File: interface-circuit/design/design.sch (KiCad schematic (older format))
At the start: 28 parts, among them J1 Raspberry_Pi_2_3, J10 Screw_Terminal_01x02, J11 Conn_01x02_Male, J12 Conn_01x02_Male, J2 Screw_Terminal_01x05, J3 Screw_Terminal_01x05, J4 Screw_Terminal_01x02, J5 Conn_01x02_Male, J6 Conn_01x02_Male, J7 Conn_01x03_Male, J8 Conn_01x03_Male, J9 Screw_Terminal_01x02, Q1 2N3904-AP, Q2 2N3904-AP, Q3 2N3904-AP, SW1 SW_SPST, SW2 SW_SPST, U1 LogicLevelConverter_BOB-08745

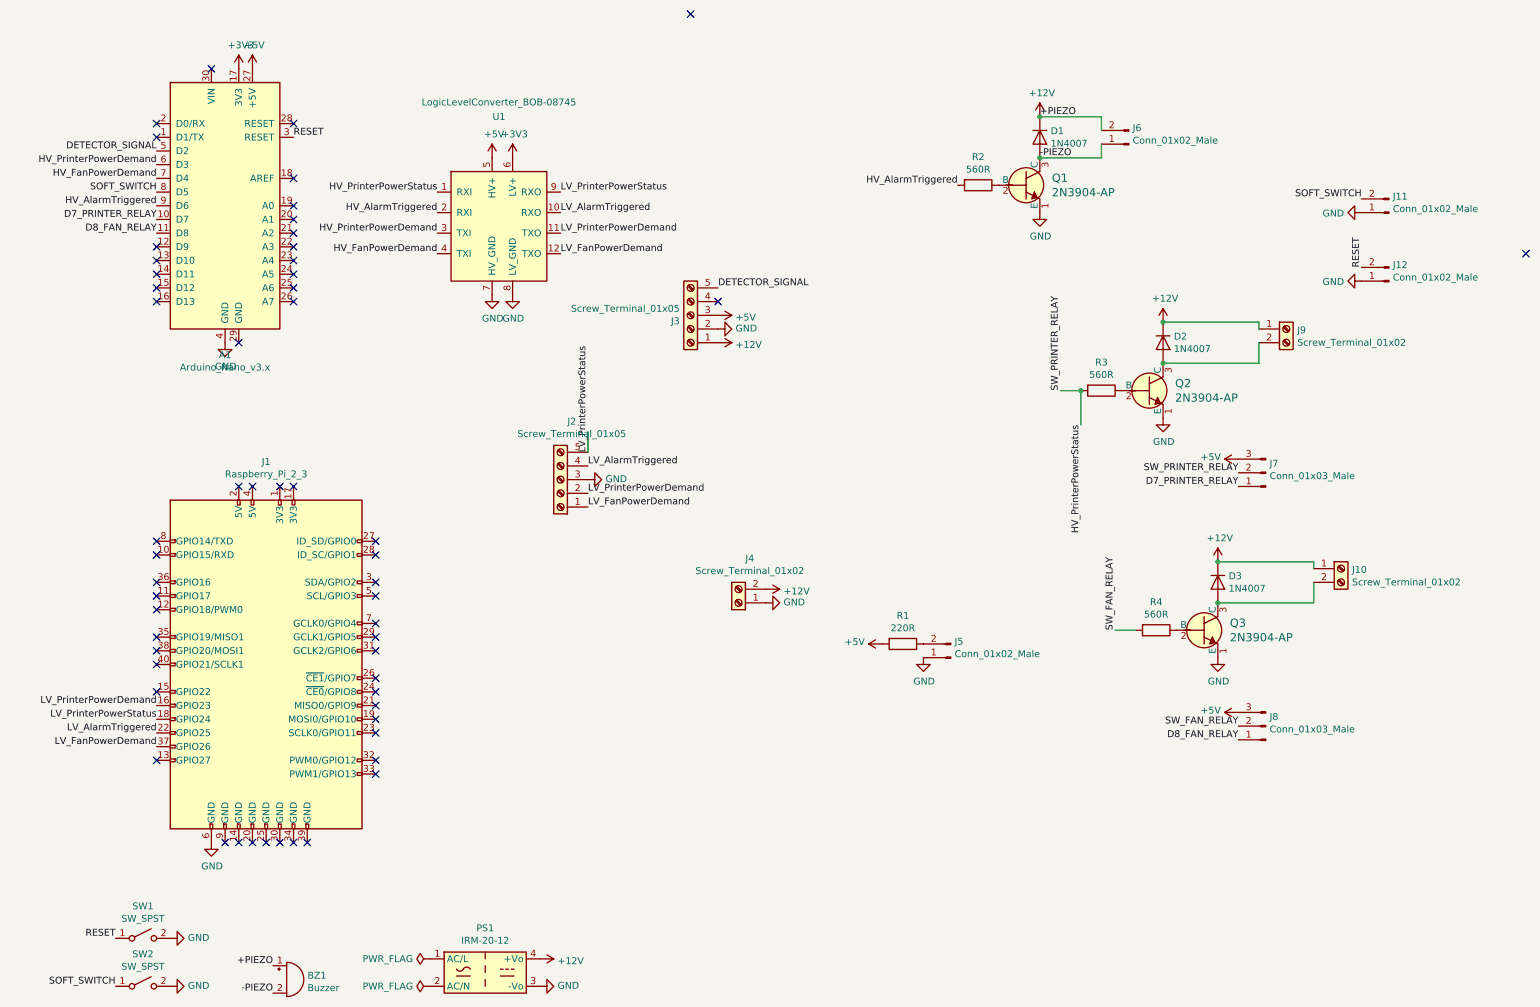
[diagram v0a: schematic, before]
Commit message: Cannot get the custom component to work, flipped in pcb new and labels associated with wrong sides
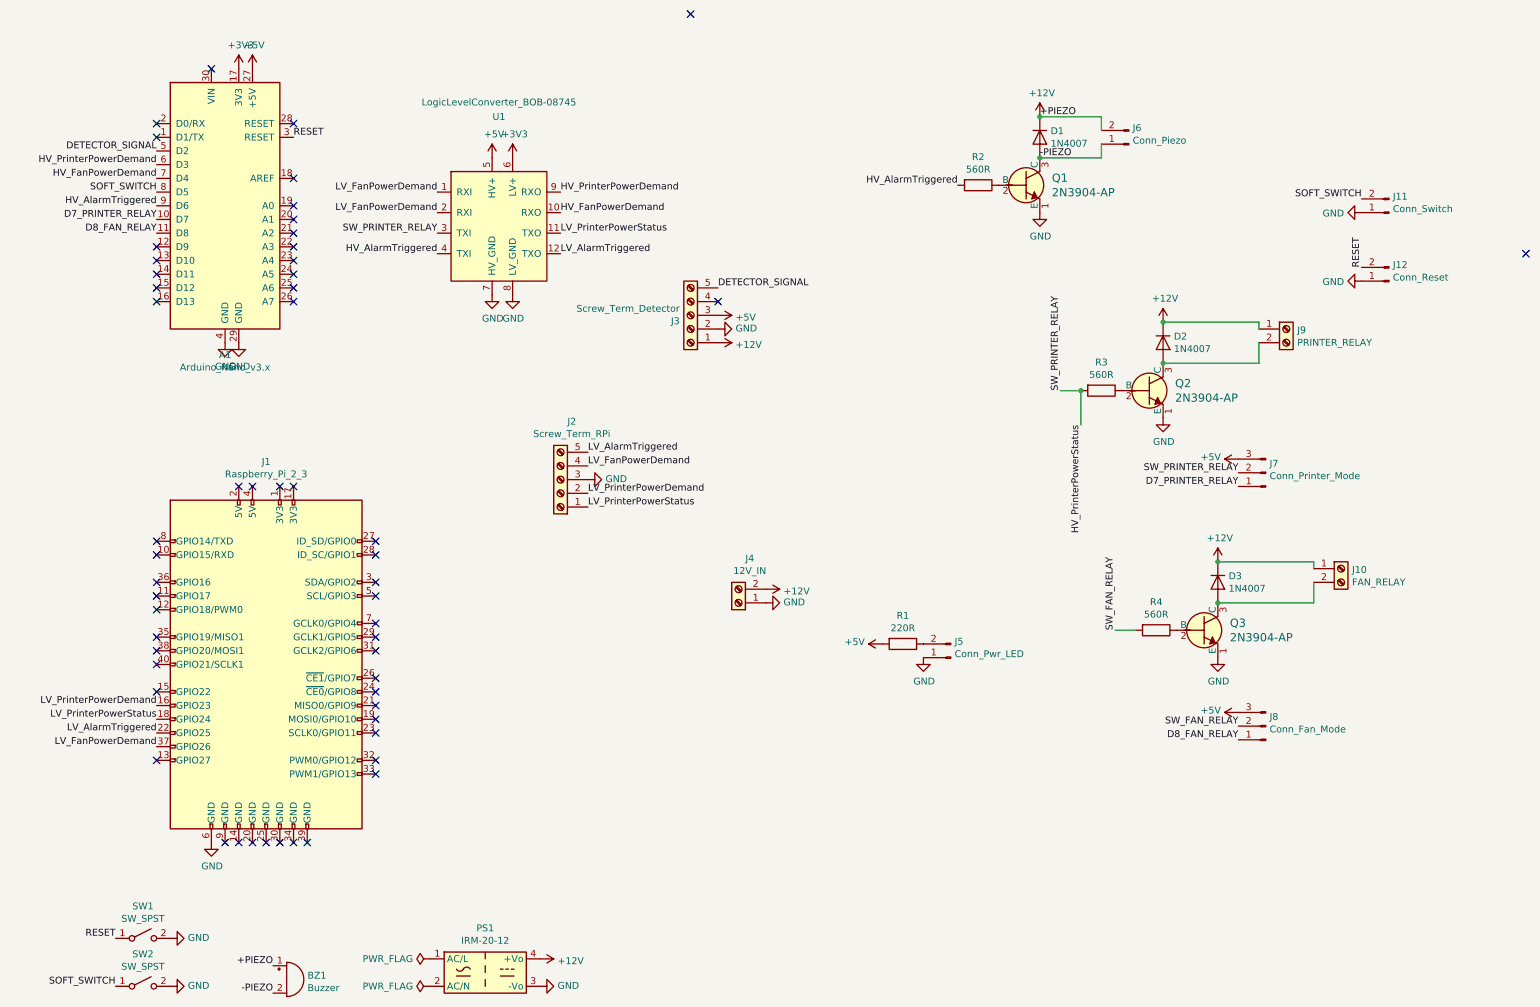
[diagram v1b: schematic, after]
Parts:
- J10: value Screw_Terminal_01x02 -> FAN_RELAY
- J11: value Conn_01x02_Male -> Conn_Switch
- J12: value Conn_01x02_Male -> Conn_Reset
- J2: value Screw_Terminal_01x05 -> Screw_Term_RPi; footprint Connectors:SCREWTERMINAL-3.5MM-5 -> digikey-footprints:Term_Block_1x5_P5.08mm
- J3: value Screw_Terminal_01x05 -> Screw_Term_Detector; footprint Connectors:SCREWTERMINAL-3.5MM-5 -> digikey-footprints:Term_Block_1x5_P5.08mm
- J4: value Screw_Terminal_01x02 -> 12V_IN
- J5: value Conn_01x02_Male -> Conn_Pwr_LED
- J6: value Conn_01x02_Male -> Conn_Piezo
- J7: value Conn_01x03_Male -> Conn_Printer_Mode
- J8: value Conn_01x03_Male -> Conn_Fan_Mode
- J9: value Screw_Terminal_01x02 -> PRINTER_RELAY
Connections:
- wire segments 16 -> 15
- no-connect marks 57 -> 56
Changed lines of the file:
@@
 Text Label 4650 3800 0    50   ~ 0
 LV_PrinterPowerDemand
-Text Label 4650 3500 1    50   ~ 0
-LV_PrinterPowerStatus
+Text Label 4650 3500 0    50   ~ 0
+LV_AlarmTriggered
 Text Label 4650 3600 0    50   ~ 0
-LV_AlarmTriggered
-Wire Wire Line
-	4650 3500 4650 3350
+LV_FanPowerDemand
 $Comp
 L power:GND #PWR013
@@
 $EndComp
 Text Label 3550 1900 2    50   ~ 0
+SW_PRINTER_RELAY
+Text Label 4450 1600 0    50   ~ 0
 HV_PrinterPowerDemand
-Text Label 4450 1600 0    50   ~ 0
-LV_PrinterPowerStatus
 Text Label 4450 1750 0    50   ~ 0
-LV_AlarmTriggered
+HV_FanPowerDemand
 $Comp
 L power:+5V #PWR07
@@
 $EndComp
 Text Label 3550 1600 2    50   ~ 0
-HV_PrinterPowerStatus
+LV_FanPowerDemand
 Text Label 3550 1750 2    50   ~ 0
-HV_AlarmTriggered
+LV_FanPowerDemand
 Text Label 4450 1900 0    50   ~ 0
-LV_PrinterPowerDemand
+LV_PrinterPowerStatus
 $Comp
 L Connector:Conn_01x02_Male J12
@@
 P 10500 2250
 F 0 "J12" H 10472 2132 50  0000 R CNN
-F 1 "Conn_01x02_Male" H 10472 2223 50  0000 R CNN
+F 1 "Conn_Reset" H 10472 2223 50  0000 R CNN
 F 2 "Connector_PinHeader_2.54mm:PinHeader_1x02_P2.54mm_Vertical" H 10500 2250 50  0001 C CNN
 F 3 "~" H 10500 2250 50  0001 C CNN
@@
 P 5400 2500
 F 0 "J3" H 5480 2542 50  0000 L CNN
-F 1 "Screw_Terminal_01x05" H 5480 2451 50  0000 L CNN
-F 2 "Connectors:SCREWTERMINAL-3.5MM-5" H 5400 2500 50  0001 C CNN
+F 1 "Screw_Term_Detector" H 5480 2451 50  0000 L CNN
+F 2 "digikey-footprints:Term_Block_1x5_P5.08mm" H 5400 2500 50  0001 C CNN
 F 3 "~" H 5400 2500 50  0001 C CNN
 	1    5400 2500
@@
 P 4450 3700
 F 0 "J2" H 4368 3275 50  0000 C CNN
-F 1 "Screw_Terminal_01x05" H 4368 3366 50  0000 C CNN
-F 2 "Connectors:SCREWTERMINAL-3.5MM-5" H 4450 3700 50  0001 C CNN
+F 1 "Screw_Term_RPi" H 4368 3366 50  0000 C CNN
+F 2 "digikey-footprints:Term_Block_1x5_P5.08mm" H 4450 3700 50  0001 C CNN
 F 3 "~" H 4450 3700 50  0001 C CNN
 	1    4450 3700
@@
 $EndComp
 Text Label 4650 3900 0    50   ~ 0
-LV_FanPowerDemand
+LV_PrinterPowerStatus
 NoConn ~ 11500 2050
 $Comp
@@
 P 10500 1750
 F 0 "J11" H 10472 1632 50  0000 R CNN
-F 1 "Conn_01x02_Male" H 10472 1723 50  0000 R CNN
+F 1 "Conn_Switch" H 10472 1723 50  0000 R CNN
 F 2 "Connector_PinHeader_2.54mm:PinHeader_1x02_P2.54mm_Vertical" H 10500 1750 50  0001 C CNN
 F 3 "~" H 10500 1750 50  0001 C CNN
@@
 P 8600 1250
 F 0 "J6" H 8572 1132 50  0000 R CNN
-F 1 "Conn_01x02_Male" H 8572 1223 50  0000 R CNN
+F 1 "Conn_Piezo" H 8572 1223 50  0000 R CNN
 F 2 "Connector_PinHeader_2.54mm:PinHeader_1x02_P2.54mm_Vertical" H 8600 1250 50  0001 C CNN
 F 3 "~" H 8600 1250 50  0001 C CNN
@@
 P 9750 2600
 F 0 "J9" H 9830 2592 50  0000 L CNN
-F 1 "Screw_Terminal_01x02" H 9830 2501 50  0000 L CNN
+F 1 "PRINTER_RELAY" H 9830 2501 50  0000 L CNN
 F 2 "Connectors:SCREWTERMINAL-5MM-2" H 9750 2600 50  0001 C CNN
 F 3 "~" H 9750 2600 50  0001 C CNN
@@
 P 10150 4350
 F 0 "J10" H 10230 4342 50  0000 L CNN
-F 1 "Screw_Terminal_01x02" H 10230 4251 50  0000 L CNN
+F 1 "FAN_RELAY" H 10230 4251 50  0000 L CNN
 F 2 "Connectors:SCREWTERMINAL-5MM-2" H 10150 4350 50  0001 C CNN
 F 3 "~" H 10150 4350 50  0001 C CNN
@@
 NoConn ~ 2500 1100
 NoConn ~ 2500 1500
-NoConn ~ 2100 2700
 NoConn ~ 1500 1100
 NoConn ~ 1500 1200
@@
 P 9600 3650
 F 0 "J7" H 9572 3582 50  0000 R CNN
-F 1 "Conn_01x03_Male" H 9572 3673 50  0000 R CNN
+F 1 "Conn_Printer_Mode" H 9572 3673 50  0000 R CNN
 F 2 "Connector_PinHeader_2.54mm:PinHeader_1x03_P2.54mm_Vertical" H 9600 3650 50  0001 C CNN
 F 3 "~" H 9600 3650 50  0001 C CNN
@@
 P 9600 5500
 F 0 "J8" H 9572 5432 50  0000 R CNN
-F 1 "Conn_01x03_Male" H 9572 5523 50  0000 R CNN
+F 1 "Conn_Fan_Mode" H 9572 5523 50  0000 R CNN
 F 2 "Connector_PinHeader_2.54mm:PinHeader_1x03_P2.54mm_Vertical" H 9600 5500 50  0001 C CNN
 F 3 "~" H 9600 5500 50  0001 C CNN
@@
 P 5750 4600
 F 0 "J4" H 5668 4275 50  0000 C CNN
-F 1 "Screw_Terminal_01x02" H 5668 4366 50  0000 C CNN
+F 1 "12V_IN" H 5668 4366 50  0000 C CNN
 F 2 "Connectors:SCREWTERMINAL-5MM-2" H 5750 4600 50  0001 C CNN
 F 3 "~" H 5750 4600 50  0001 C CNN
@@
 P 7300 5000
 F 0 "J5" H 7272 4882 50  0000 R CNN
-F 1 "Conn_01x02_Male" H 7272 4973 50  0000 R CNN
+F 1 "Conn_Pwr_LED" H 7272 4973 50  0000 R CNN
 F 2 "Connector_PinHeader_2.54mm:PinHeader_1x02_P2.54mm_Vertical" H 7300 5000 50  0001 C CNN
 F 3 "~" H 7300 5000 50  0001 C CNN
@@
 LV_FanPowerDemand
 Text Label 4450 2050 0    50   ~ 0
-LV_FanPowerDemand
+LV_AlarmTriggered
 Text Label 3550 2050 2    50   ~ 0
-HV_FanPowerDemand
+HV_AlarmTriggered
 Text Label 7350 1550 2    50   ~ 0
 HV_AlarmTriggered
@@
 Text Label 1200 7050 2    50   ~ 0
 RESET
+$Comp
+L power:GND #PWR0101
+U 1 1 5CE49583
+P 2100 2700
+F 0 "#PWR0101" H 2100 2450 50  0001 C CNN
+F 1 "GND" H 2105 2527 50  0000 C CNN
+F 2 "" H 2100 2700 50  0001 C CNN
+F 3 "" H 2100 2700 50  0001 C CNN
+	1    2100 2700
+	1    0    0    -1
+$EndComp
 $EndSCHEMATC

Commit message: Done with manual routing
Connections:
- net +5V: now also J7.2 (Pin_2), J8.2 (Pin_2); no longer J7.3 (Pin_3), J8.3 (Pin_3)
- net HV_AlarmTriggered: now also U1.2 (RXI); no longer U1.4 (TXI)
- net HV_FanPowerDemand: now also U1.12 (TXO); no longer U1.10 (RXO)
- net HV_PrinterPowerDemand: now also U1.11 (TXO); no longer U1.9 (RXO)
- net HV_PrinterPowerStatus: now also J7.3 (Pin_3), U1.1 (RXI); no longer J7.2 (Pin_2), U1.3 (TXI)
- net LV_AlarmTriggered: now also J2.4 (Pin_4), U1.10 (RXO); no longer J2.5 (Pin_5), U1.12 (TXO)
- net LV_FanPowerDemand: now also J2.5 (Pin_5), U1.4 (TXI); no longer J2.4 (Pin_4), U1.1 (RXI), U1.2 (RXI)
- net LV_PrinterPowerDemand: now also J2.1 (Pin_1), U1.3 (TXI); no longer J2.2 (Pin_2)
- net LV_PrinterPowerStatus: now also J2.2 (Pin_2), U1.9 (RXO); no longer J2.1 (Pin_1), U1.11 (TXO)
- net SW_FAN_RELAY: now also J8.3 (Pin_3); no longer J8.2 (Pin_2)
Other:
- moved on the sheet: J7, J8
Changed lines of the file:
@@
 NoConn ~ 2600 6350
 Text Label 4650 3800 0    50   ~ 0
-LV_PrinterPowerDemand
+LV_PrinterPowerStatus
 Text Label 4650 3500 0    50   ~ 0
+LV_FanPowerDemand
+Text Label 4650 3600 0    50   ~ 0
 LV_AlarmTriggered
-Text Label 4650 3600 0    50   ~ 0
-LV_FanPowerDemand
 $Comp
 L power:GND #PWR013
@@
 $EndComp
 Text Label 3550 1900 2    50   ~ 0
-SW_PRINTER_RELAY
+LV_PrinterPowerDemand
 Text Label 4450 1600 0    50   ~ 0
-HV_PrinterPowerDemand
+LV_PrinterPowerStatus
 Text Label 4450 1750 0    50   ~ 0
-HV_FanPowerDemand
+LV_AlarmTriggered
 $Comp
 L power:+5V #PWR07
@@
 $EndComp
 Text Label 3550 1600 2    50   ~ 0
-LV_FanPowerDemand
+SW_PRINTER_RELAY
 Text Label 3550 1750 2    50   ~ 0
-LV_FanPowerDemand
+HV_AlarmTriggered
 Text Label 4450 1900 0    50   ~ 0
-LV_PrinterPowerStatus
+HV_PrinterPowerDemand
 $Comp
 L Connector:Conn_01x02_Male J12
@@
 $EndComp
 Text Label 4650 3900 0    50   ~ 0
-LV_PrinterPowerStatus
+LV_PrinterPowerDemand
 NoConn ~ 11500 2050
 $Comp
@@
 L Connector:Conn_01x03_Male J7
 U 1 1 5CCAE331
-P 9600 3650
-F 0 "J7" H 9572 3582 50  0000 R CNN
-F 1 "Conn_Printer_Mode" H 9572 3673 50  0000 R CNN
-F 2 "Connector_PinHeader_2.54mm:PinHeader_1x03_P2.54mm_Vertical" H 9600 3650 50  0001 C CNN
-F 3 "~" H 9600 3650 50  0001 C CNN
-	1    9600 3650
-	-1   0    0    1
-$EndComp
-$Comp
-L power:+5V #PWR027
-U 1 1 5CCAF476
-P 9400 3550
-F 0 "#PWR027" H 9400 3400 50  0001 C CNN
-F 1 "+5V" V 9415 3678 50  0000 L CNN
-F 2 "" H 9400 3550 50  0001 C CNN
-F 3 "" H 9400 3550 50  0001 C CNN
-	1    9400 3550
-	0    -1   -1   0
-$EndComp
-Text Label 9400 3750 2    50   ~ 0
+P 9550 3700
+F 0 "J7" H 9522 3632 50  0000 R CNN
+F 1 "Conn_Printer_Mode" H 9522 3723 50  0000 R CNN
+F 2 "Connector_PinHeader_2.54mm:PinHeader_1x03_P2.54mm_Vertical" H 9550 3700 50  0001 C CNN
+F 3 "~" H 9550 3700 50  0001 C CNN
+	1    9550 3700
+	1    0    0    -1
+$EndComp
+Text Label 9750 3600 0    50   ~ 0
 D7_PRINTER_RELAY
 Text Label 8100 3050 1    50   ~ 0
 SW_PRINTER_RELAY
-Text Label 9400 3650 2    50   ~ 0
-SW_PRINTER_RELAY
-$Comp
-L Connector:Conn_01x03_Male J8
-U 1 1 5CCBFC14
-P 9600 5500
-F 0 "J8" H 9572 5432 50  0000 R CNN
-F 1 "Conn_Fan_Mode" H 9572 5523 50  0000 R CNN
-F 2 "Connector_PinHeader_2.54mm:PinHeader_1x03_P2.54mm_Vertical" H 9600 5500 50  0001 C CNN
-F 3 "~" H 9600 5500 50  0001 C CNN
-	1    9600 5500
-	-1   0    0    1
-$EndComp
-$Comp
-L power:+5V #PWR028
-U 1 1 5CCBFC1E
-P 9400 5400
-F 0 "#PWR028" H 9400 5250 50  0001 C CNN
-F 1 "+5V" V 9415 5528 50  0000 L CNN
-F 2 "" H 9400 5400 50  0001 C CNN
-F 3 "" H 9400 5400 50  0001 C CNN
-	1    9400 5400
-	0    -1   -1   0
-$EndComp
-Text Label 9400 5600 2    50   ~ 0
+Text Label 9400 5500 0    50   ~ 0
 D8_FAN_RELAY
-Text Label 9400 5500 2    50   ~ 0
-SW_FAN_RELAY
 $Comp
 L Connector:Screw_Terminal_01x02 J4
@@
 LV_FanPowerDemand
 Text Label 4450 2050 0    50   ~ 0
-LV_AlarmTriggered
+HV_FanPowerDemand
 Text Label 3550 2050 2    50   ~ 0
-HV_AlarmTriggered
+LV_FanPowerDemand
 Text Label 7350 1550 2    50   ~ 0
 HV_AlarmTriggered
@@
 	1    0    0    -1
 $EndComp
+$Comp
+L Connector:Conn_01x03_Male J8
+U 1 1 5CCBFC14
+P 9200 5600
+F 0 "J8" H 9172 5532 50  0000 R CNN
+F 1 "Conn_Fan_Mode" H 9172 5623 50  0000 R CNN
+F 2 "Connector_PinHeader_2.54mm:PinHeader_1x03_P2.54mm_Vertical" H 9200 5600 50  0001 C CNN
+F 3 "~" H 9200 5600 50  0001 C CNN
+	1    9200 5600
+	1    0    0    -1
+$EndComp
+$Comp
+L power:+5V #PWR0102
+U 1 1 5CC5D628
+P 9400 5600
+F 0 "#PWR0102" H 9400 5450 50  0001 C CNN
+F 1 "+5V" V 9415 5728 50  0000 L CNN
+F 2 "" H 9400 5600 50  0001 C CNN
+F 3 "" H 9400 5600 50  0001 C CNN
+	1    9400 5600
+	0    1    1    0
+$EndComp
+Text Label 9400 5700 0    50   ~ 0
+SW_FAN_RELAY
+Text Label 9750 3800 0    50   ~ 0
+SW_PRINTER_RELAY
+$Comp
+L power:+5V #PWR?
+U 1 1 5CC658C6
+P 9750 3700
+F 0 "#PWR?" H 9750 3550 50  0001 C CNN
+F 1 "+5V" V 9765 3828 50  0000 L CNN
+F 2 "" H 9750 3700 50  0001 C CNN
+F 3 "" H 9750 3700 50  0001 C CNN
+	1    9750 3700
+	0    1    1    0
+$EndComp
 $EndSCHEMATC
